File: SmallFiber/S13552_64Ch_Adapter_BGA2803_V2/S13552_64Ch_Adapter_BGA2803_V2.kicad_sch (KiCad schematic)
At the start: 11 parts, among them J1 ERM6-30-01.5-L-DV-A-K-TR, J2 ERM6-30-01.5-L-DV-A-K-TR

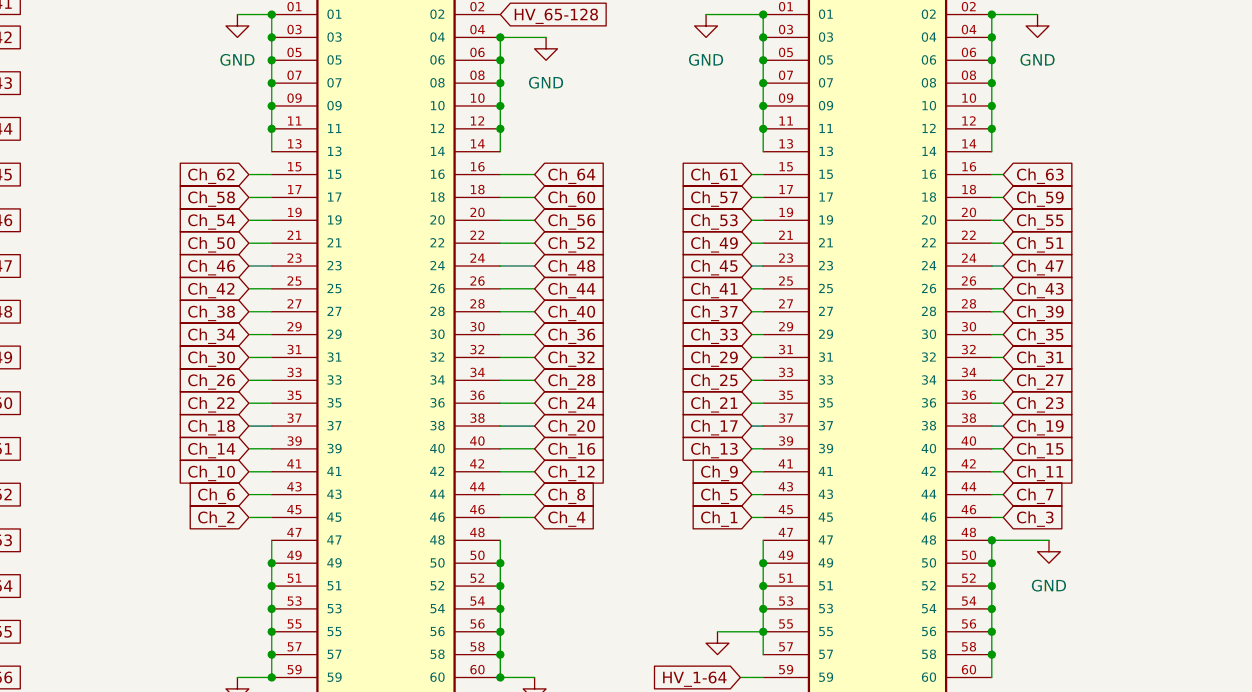
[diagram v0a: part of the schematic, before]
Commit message: Update PCB: resistor values, datasheet fields, and netlist
Changed several resistor values from 50 to 150 in the S13552_64Ch_Adapter_BGA2803_V2.kicad_pcb file, updated empty datasheet fields to '~', and corrected sheetfile references. Added new unconnected nets for J1 and J2 connectors. Also includes new and updated backup files, and adds new SPICE simulation files.
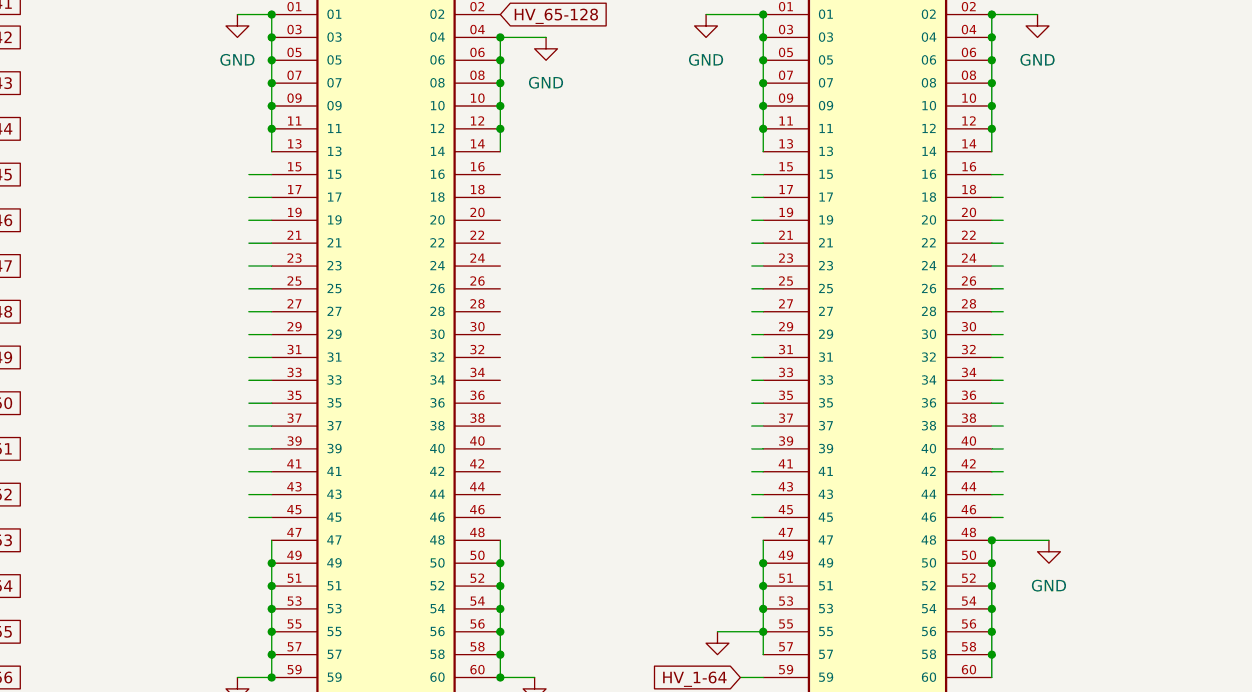
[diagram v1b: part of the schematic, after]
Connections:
- net Ch_1: no longer J2.45
- net Ch_10: no longer J1.41
- net Ch_11: no longer J2.42
- net Ch_12: no longer J1.42
- net Ch_13: no longer J2.39
- net Ch_14: no longer J1.39
- net Ch_15: no longer J2.40
- net Ch_16: no longer J1.40
- net Ch_17: no longer J2.37
- net Ch_18: no longer J1.37
- net Ch_19: no longer J2.38
- net Ch_2: no longer J1.45
- net Ch_20: no longer J1.38
- net Ch_21: no longer J2.35
- net Ch_22: no longer J1.35
- net Ch_23: no longer J2.36
- net Ch_24: no longer J1.36
- net Ch_25: no longer J2.33
- net Ch_26: no longer J1.33
- net Ch_27: no longer J2.34
- net Ch_28: no longer J1.34
- net Ch_29: no longer J2.31
- net Ch_3: no longer J2.46
- net Ch_30: no longer J1.31
- net Ch_31: no longer J2.32
- net Ch_32: no longer J1.32
- net Ch_33: no longer J2.29
- net Ch_34: no longer J1.29
- net Ch_35: no longer J2.30
- net Ch_36: no longer J1.30
- net Ch_37: no longer J2.27
- net Ch_38: no longer J1.27
- net Ch_39: no longer J2.28
- net Ch_4: no longer J1.46
- net Ch_40: no longer J1.28
- net Ch_41: no longer J2.25
- net Ch_42: no longer J1.25
- net Ch_43: no longer J2.26
- net Ch_44: no longer J1.26
- net Ch_45: no longer J2.23
- net Ch_46: no longer J1.23
- net Ch_47: no longer J2.24
- net Ch_48: no longer J1.24
- net Ch_49: no longer J2.21
- net Ch_5: no longer J2.43
- net Ch_50: no longer J1.21
- net Ch_51: no longer J2.22
- net Ch_52: no longer J1.22
- net Ch_53: no longer J2.19
- net Ch_54: no longer J1.19
- net Ch_55: no longer J2.20
- net Ch_56: no longer J1.20
- net Ch_57: no longer J2.17
- net Ch_58: no longer J1.17
- net Ch_59: no longer J2.18
- net Ch_6: no longer J1.43
- net Ch_60: no longer J1.18
- net Ch_61: no longer J2.15
- net Ch_62: no longer J1.15
- net Ch_63: no longer J2.16
- net Ch_64: no longer J1.16
- net Ch_7: no longer J2.44
- net Ch_8: no longer J1.44
- net Ch_9: no longer J2.41
